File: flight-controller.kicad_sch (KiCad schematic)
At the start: 16 parts, among them J1 USB_C_Receptacle_USB2.0_16P, SW1 SW_Push, U1 ESP32-C3-WROOM-02, U2 MPU-6050, U3 AMS1117-3.3

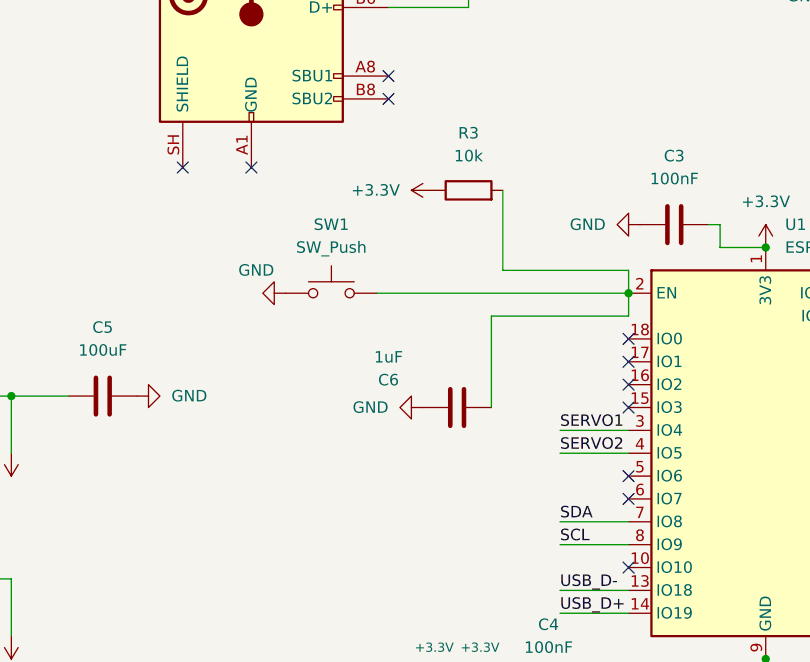
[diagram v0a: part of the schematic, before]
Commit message: - Redid all the traces from scratch with a much clearer design plan - Much cleaner paths, large and thick powerlines, thinner and more direct signal lines Ground plate works better now
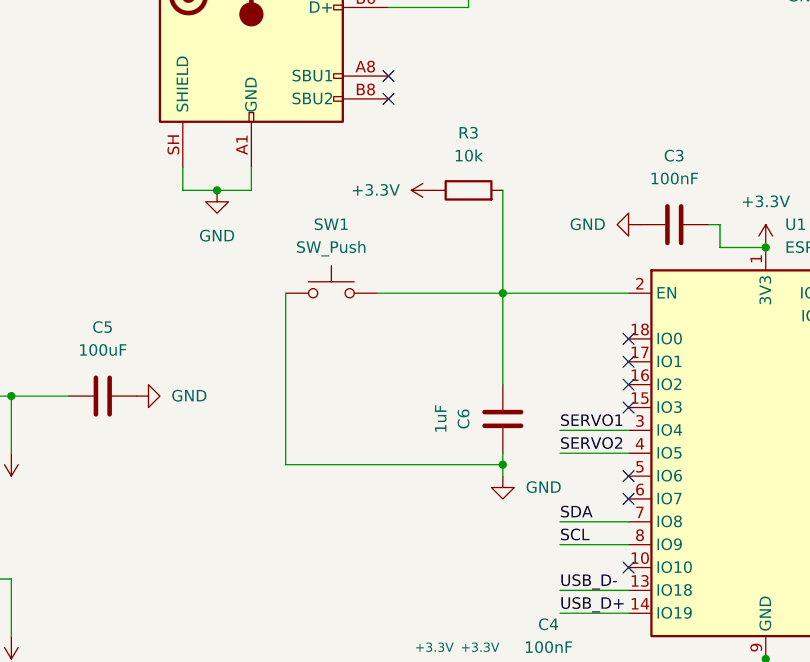
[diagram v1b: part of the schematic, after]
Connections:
- net GND: now also J1.A1 (GND), J1.A12 (GND), J1.B1 (GND), J1.B12 (GND), J1.SH (SHIELD)
- no-connect marks 21 -> 19
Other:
- moved on the sheet: C6

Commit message: Improvements to schematics and PCB design. - GND always points down - Power always points up - Adjusted powerlines
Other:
- moved on the sheet: C3

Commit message: Restructued Layout slightly and added new BOM
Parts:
- added U4: ICM-20602, Package_LGA:LGA-16_3x3mm_P0.5mm_LayoutBorder3x5y, symbol Sensor_Motion:ICM-20602
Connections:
- new net: U4.10 (GND), U4.11 (GND), U4.12 (GND), U4.13 (GND), U4.15 (GND), U4.9 (GND)
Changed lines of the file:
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@@
+	)
+	(symbol
+		(lib_id "Sensor_Motion:ICM-20602")
+		(at 88.9 165.1 0)
+		(unit 1)
+		(body_style 1)
+		(exclude_from_sim no)
+		(in_bom yes)
+		(on_board yes)
+		(in_pos_files yes)
+		(dnp no)
+		(fields_autoplaced yes)
+		(property "Reference" "U4"
+			(at 91.0433 177.8 0)
+			(show_name no)
+			(do_not_autoplace no)
+			(effects
+				(font
+					(size 1.27 1.27)
+				)
+				(justify left)
+			)
+		)
+		(property "Value" "ICM-20602"
+			(at 91.0433 180.34 0)
+			(show_name no)
+			(do_not_autoplace no)
+			(effects
+				(font
+					(size 1.27 1.27)
+				)
+				(justify left)
+			)
+		)
+		(property "Footprint" "Package_LGA:LGA-16_3x3mm_P0.5mm_LayoutBorder3x5y"
+			(at 88.9 158.75 0)
+			(hide yes)
+			(show_name no)
+			(do_not_autoplace no)
+			(effects
+				(font
+					(size 1.27 1.27)
+				)
+			)
+		)
+		(property "Datasheet" "http://www.invensense.com/wp-content/uploads/2016/10/DS-000176-ICM-20602-v1.0.pdf"
+			(at 90.17 140.97 0)
+			(hide yes)
+			(show_name no)
+			(do_not_autoplace no)
+			(effects
+				(font
+					(size 1.27 1.27)
+				)
+			)
+		)
+		(property "Description" "High performance 6-Axis MEMS motion tracking, SPI/I2C interface, LGA-16"
+			(at 88.9 165.1 0)
+			(hide yes)
+			(show_name no)
+			(do_not_autoplace no)
+			(effects
+				(font
+					(size 1.27 1.27)
+				)
+			)
+		)
+		(pin "12"
+		)
+		(pin "10"
+		)
+		(pin "15"
+		)
+		(pin "1"
+		)
+		(pin "9"
+		)
+		(pin "2"
+		)
+		(pin "13"
+		)
+		(pin "14"
+		)
+		(pin "11"
+		)
+		(pin "8"
+		)
+		(pin "16"
+		)
+		(pin "7"
+		)
+		(pin "6"
+		)
+		(pin "3"
+		)
+		(pin "4"
+		)
+		(pin "5"
+		)
+		(instances
+			(project "flight-controller"
+				(path "/d43447dc-247a-4cd0-9df8-02a6da79b4fe"
+					(reference "U4")
+					(unit 1)
+				)
+			)
+		)
 	)
 	(symbol

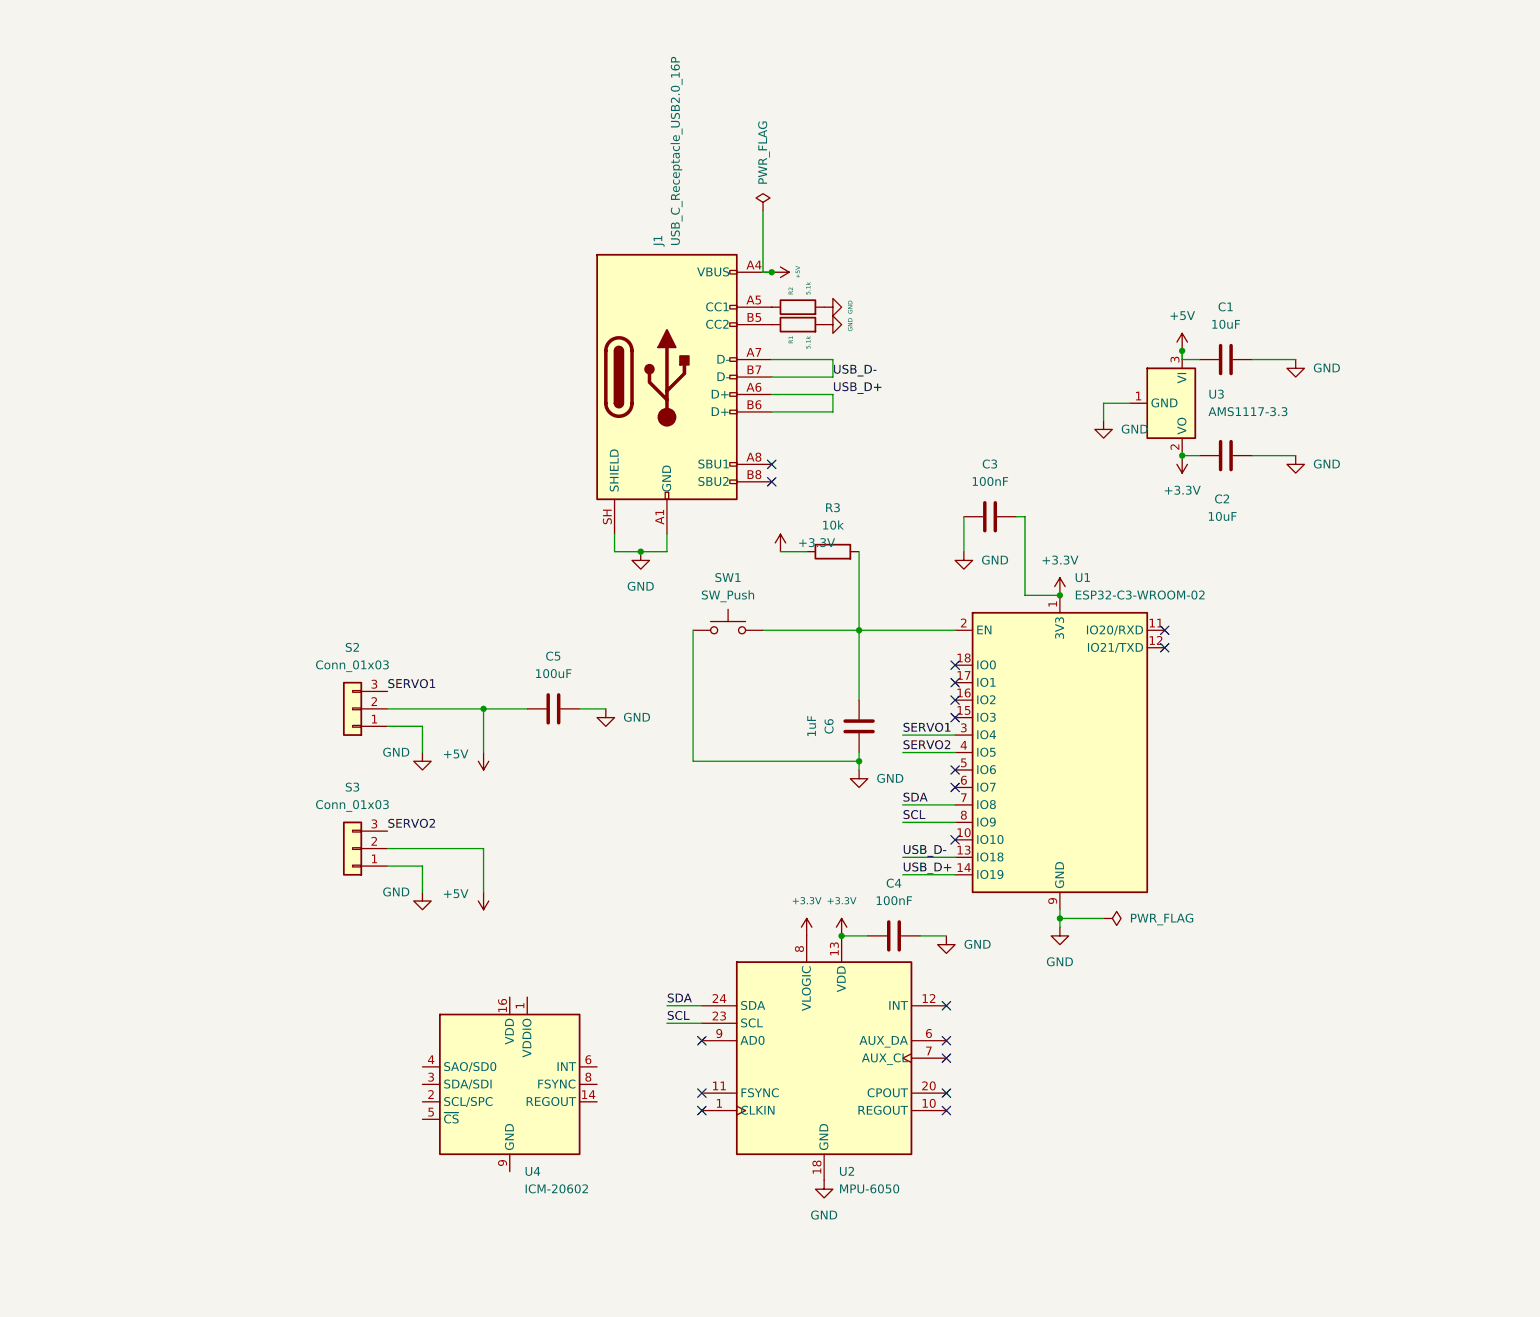
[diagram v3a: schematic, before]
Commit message: Added a Power LED indicator Added a Status LED indicator Replaced MPU6050 with cheaper and more modern ICM-20602
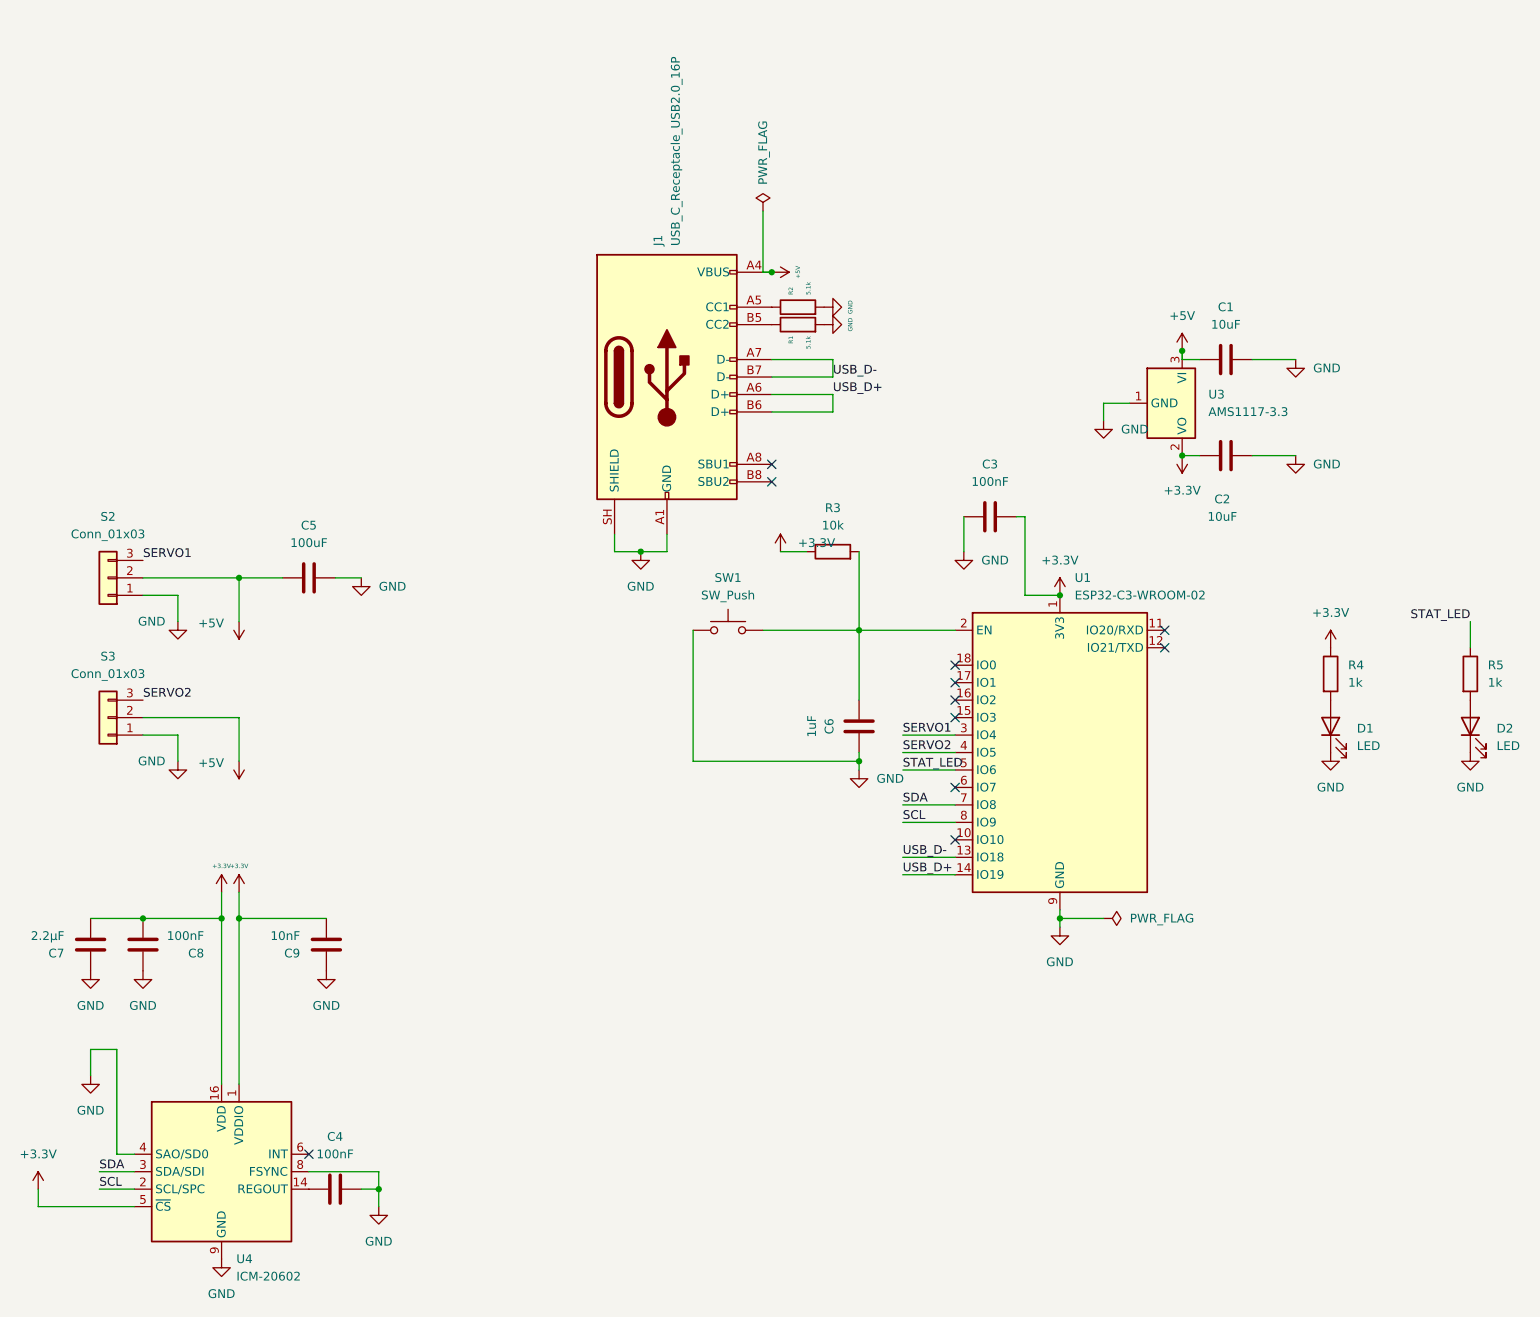
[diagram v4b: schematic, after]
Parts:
- removed U2: MPU-6050, Sensor_Motion:InvenSense_QFN-24_4x4mm_P0.5mm, symbol Sensor_Motion:MPU-6050
- added C7: 2.2µF, symbol Device:C
- added C8: 100nF, symbol Device:C
- added C9: 10nF, symbol Device:C
- added D1, D2: LED, symbol Device:LED
- added R4, R5: 1k, symbol Device:R
- C4: footprint Capacitor_SMD:C_0805_2012Metric -> (none)
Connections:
- net +3.3V: now also U4.1 (VDDIO), U4.16 (VDD), U4.5 (~{CS}), C7.2, C8.2, C9.2, R4.1; no longer C4.1
- net GND: now also C4.1, U4.10 (GND), U4.11 (GND), U4.12 (GND), U4.13 (GND), U4.15 (GND), U4.4 (SAO/SD0), U4.8 (FSYNC), U4.9 (GND), C7.1, C8.1, C9.1, D1.1 (K), D2.1 (K); no longer C4.2
- net SCL: now also U4.2 (SCL/SPC)
- net SDA: now also U4.3 (SDA/SDI)
- net at U4.14 (REGOUT): now also C4.2
- net STAT_LED: now reaches U1.5 (IO6)
- net STAT_LED: now also R5.1
- new net: D1.2 (A), R4.2
- new net: D2.2 (A), R5.2
- no-connect marks 19 -> 11
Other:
- title: (none) -> Mirage 
- moved on the sheet: C5, S2, S3

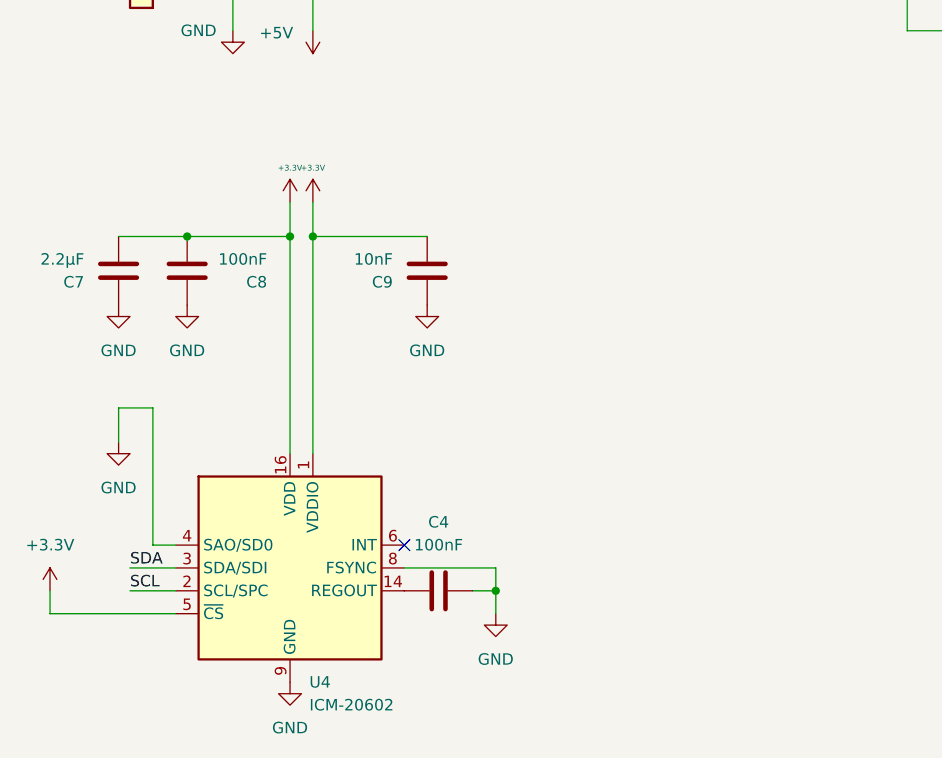
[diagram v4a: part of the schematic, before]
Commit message: Added pull up resistors to SDA and SCL pins
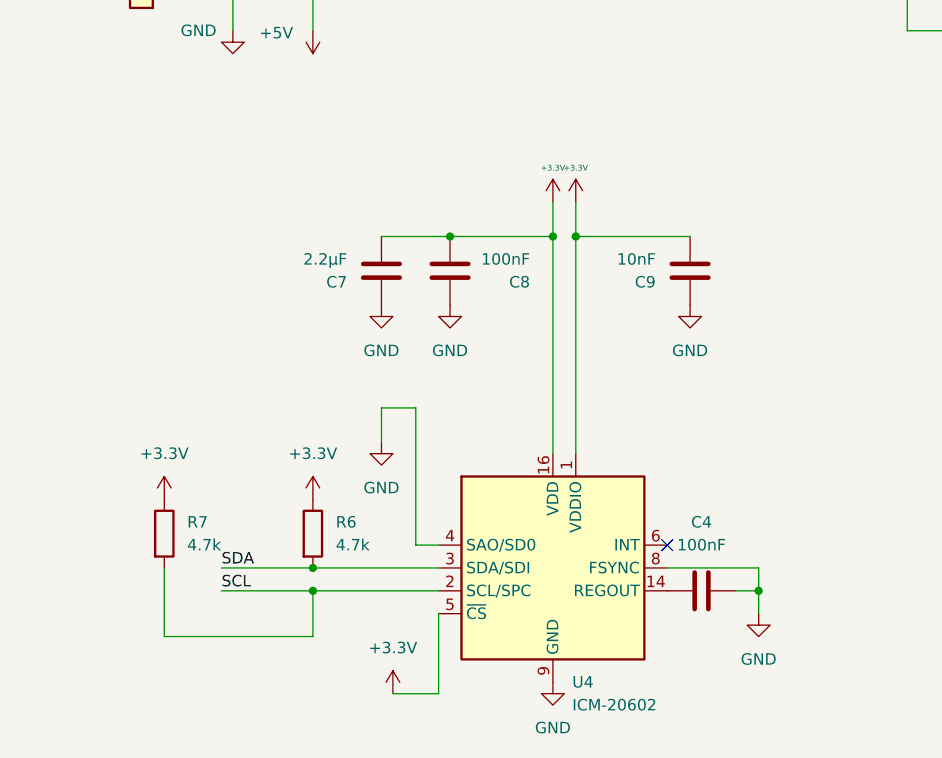
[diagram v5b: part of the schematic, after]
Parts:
- added R6, R7: 4.7k, Resistor_SMD:R_0805_2012Metric, symbol Device:R
- C4, C7, C8, C9: footprint (none) -> Capacitor_SMD:C_0805_2012Metric
- D1, D2: footprint (none) -> LED_SMD:LED_0805_2012Metric
- R4, R5: footprint (none) -> Resistor_SMD:R_0805_2012Metric
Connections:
- net +3.3V: now also R6.1, R7.1
- net SCL: now also R7.2
- net SDA: now also R6.2
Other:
- moved on the sheet: C4, C7, C8, C9, U4

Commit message: Redone the layout of the PCB to incorporate the Power LED and Status LED Also removed MPU6050 and replaced with IMC 20602 and relevant capacitors Added 2 pull up resistors to SCL and SDA lines
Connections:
- net STAT_LED: now also U1.10 (IO10); no longer U1.5 (IO6)
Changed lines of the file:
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@@
-	)
-	(no_connect
-		(at 153.67 129.54)
 	)
 	(no_connect
@@
 		(at 88.9 175.26)
 	)
+	(no_connect
+		(at 153.67 119.38)
+	)
 	(wire
 		(pts
@@
 	(wire
 		(pts
+			(xy 146.05 129.54) (xy 153.67 129.54)
+		)
+		(stroke
+			(width 0)
+			(type default)
+		)
+	)
+	(wire
+		(pts
 			(xy 99.06 177.8) (xy 99.06 180.34)
 		)
@@
 		(pts
 			(xy 49.53 91.44) (xy 55.88 91.44)
-		)
-		(stroke
-			(width 0)
-			(type default)
-		)
-	)
-	(wire
-		(pts
-			(xy 146.05 119.38) (xy 153.67 119.38)
 		)
 		(stroke
@@
 		)
 	)
+	(label "STAT_LED"
+		(at 146.05 129.54 0)
+		(effects
+			(font
+				(size 1.27 1.27)
+			)
+			(justify left bottom)
+		)
+	)
 	(label "SCL"
 		(at 39.37 180.34 0)
@@
 		(effects
 			(font
-				(size 1.27 1.27)
-			)
-			(justify left bottom)
-		)
-	)
-	(label "STAT_LED"
-		(at 146.05 119.38 0)
-		(effects
-			(font
